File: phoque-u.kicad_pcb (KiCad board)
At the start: 4 copper layers, 212.3 x 75.4 mm, 54 parts, among them J1 18…56 V, J2 On / Off, J3 3.3…24 V, Q1 SiR120DP, Q2 SiR120DP, Q3 SiR120DP, Q4 SiR120DP, SW1 Remote, SW2 Voltage select, T1 320 µ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

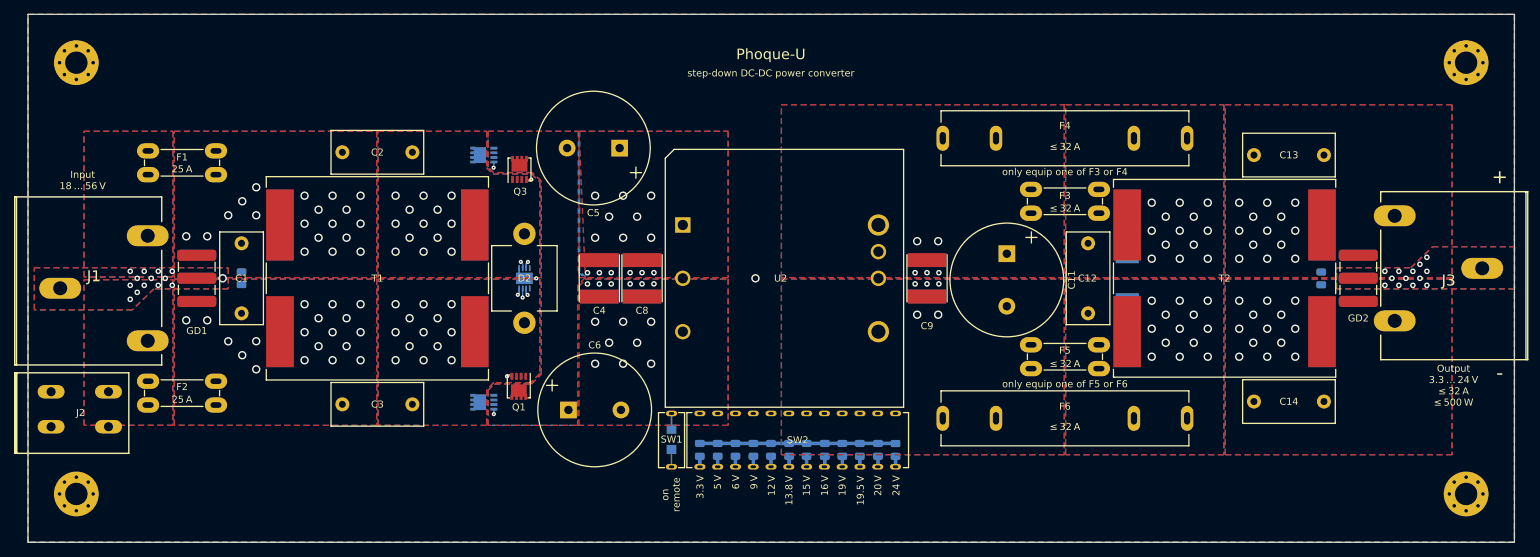
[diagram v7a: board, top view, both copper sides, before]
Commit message: Finalise silkscreen
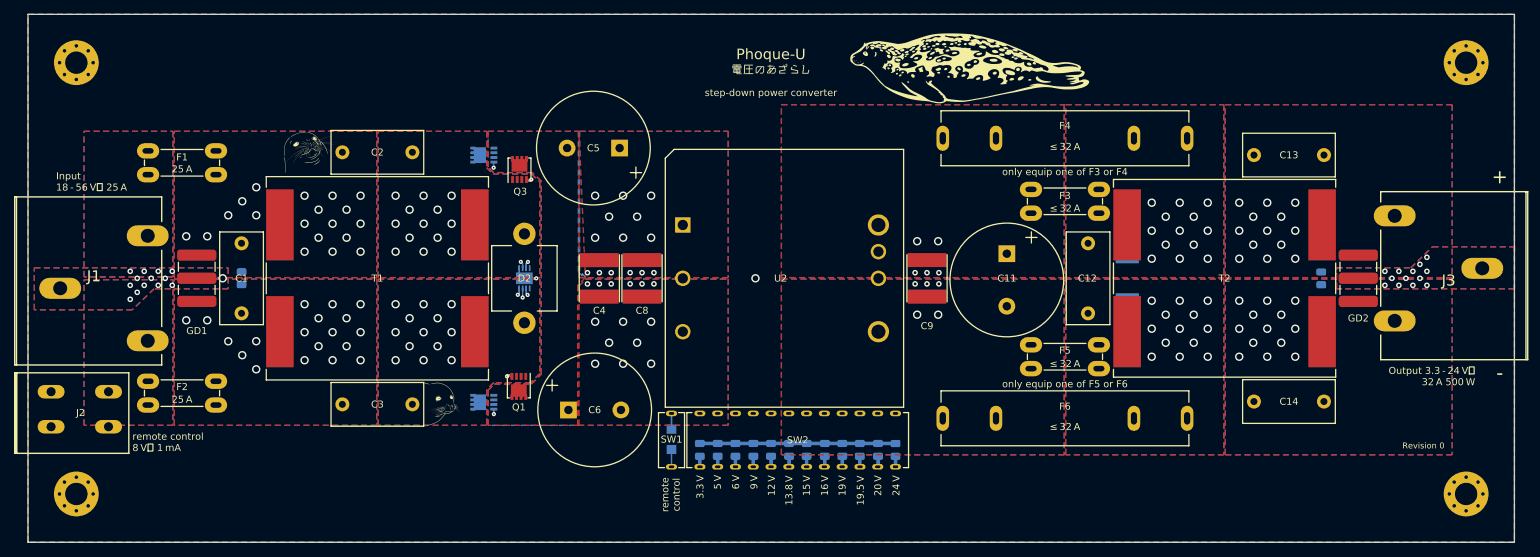
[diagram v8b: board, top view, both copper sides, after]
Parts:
- added G***: seal, LOGO, F.Cu at (83.2, 80.8)
- added G***: seal, LOGO, F.Cu at (101.1, 116.1)
- added G***: seal, LOGO, F.Cu at (177.5, 68.5)
- added G***: 電圧のあざらし, LOGO, F.Cu at (149.1, 68.6)
- added G***: LOGO, LOGO, B.Cu at (137.6, 70.1)
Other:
- board text added: "Designed in 2022 by Mikael Voss This work may be used under the terms of the strictly‐reciprocative CERN Open Hardware Licence (CERN-OHL-S) version 2."
- board text added: "Input 18 - 56 V⎓ 25 A"
- board text added: "Output 3.3 - 24 V⎓ 32 A 500 W"
- board text added: "Revision 0"
- board text added: "remote control"
- board text added: "remote control 8 V⎓ 1 mA"
- board text added: "step‐down power converter"
- board text removed: "Copyright 2022 Mikael Voss This work may be used under the terms of the strictly‐reciprocative CERN Open Hardware Licence (CERN-OHL-S) version 2."
- board text removed: "Input 18 … 56 V"
- board text removed: "Output 3.3 … 24 V ≤ 32 A ≤ 500 W"
- board text removed: "on remote"
- board text removed: "remote on/off"
- board text removed: "step‐down DC‐DC power converter"
